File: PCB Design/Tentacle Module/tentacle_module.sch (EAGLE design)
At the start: 53 parts, among them IC1 5V, T1 NTD5867NL, T2 NTD5867NL, T3 NTD5867NL, T4 NTD5867NL, X3 RJ45-8X, X4 RJ45-8X

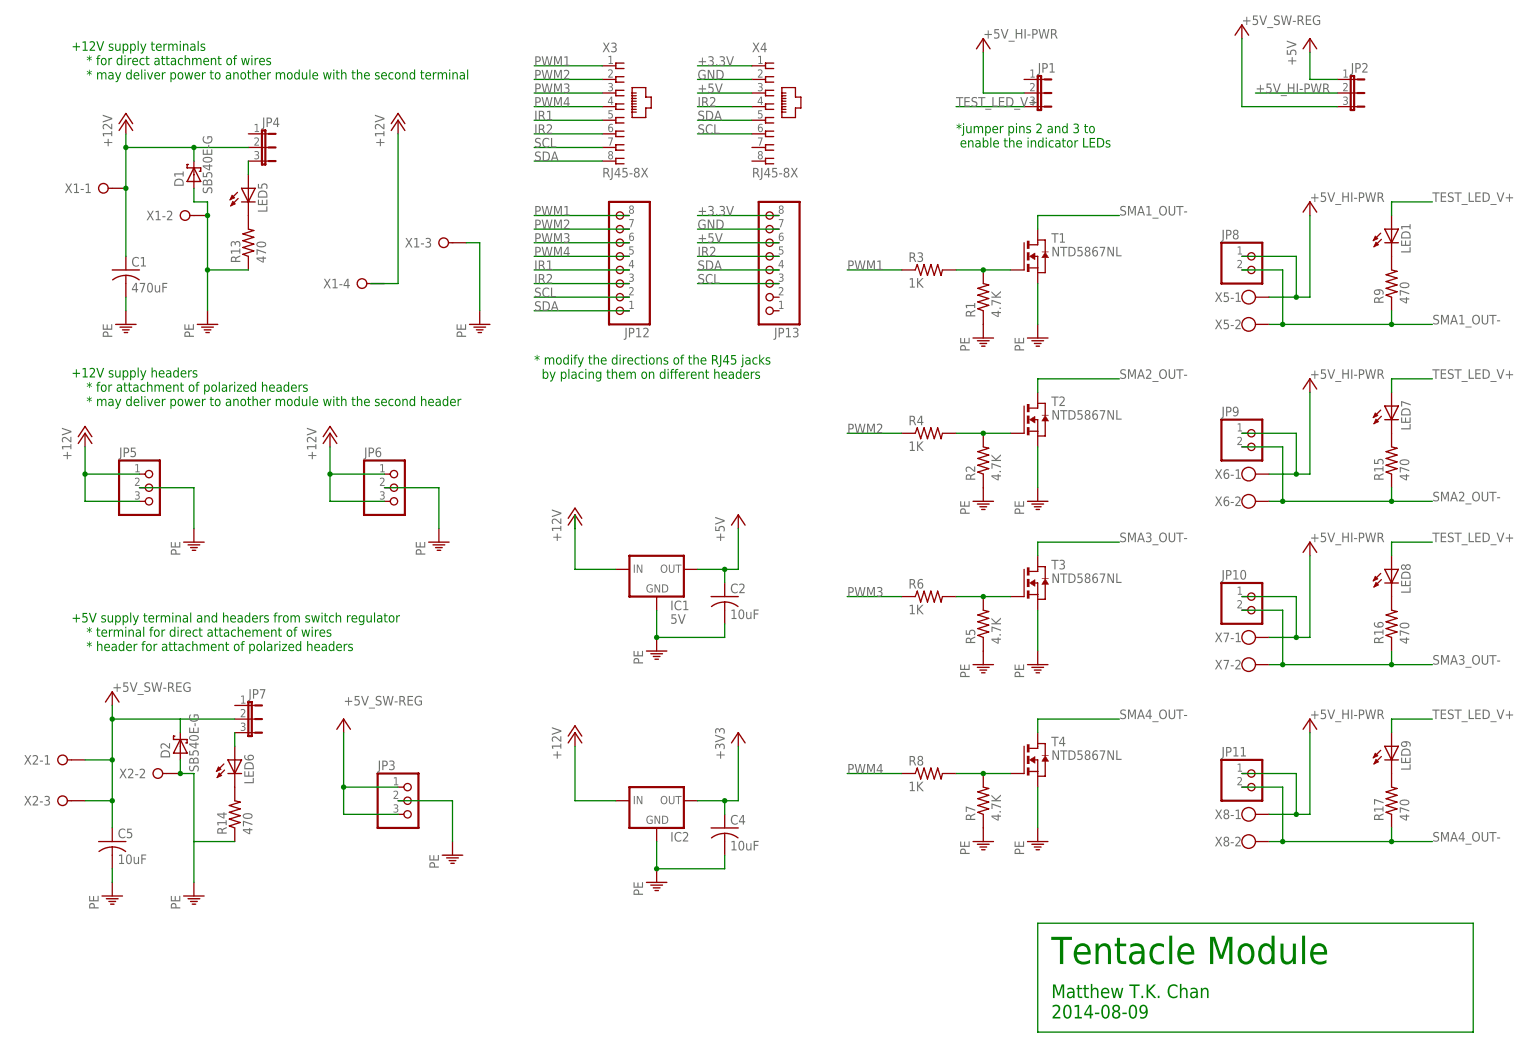
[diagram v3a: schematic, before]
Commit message: Updated the Tentacle module schematic
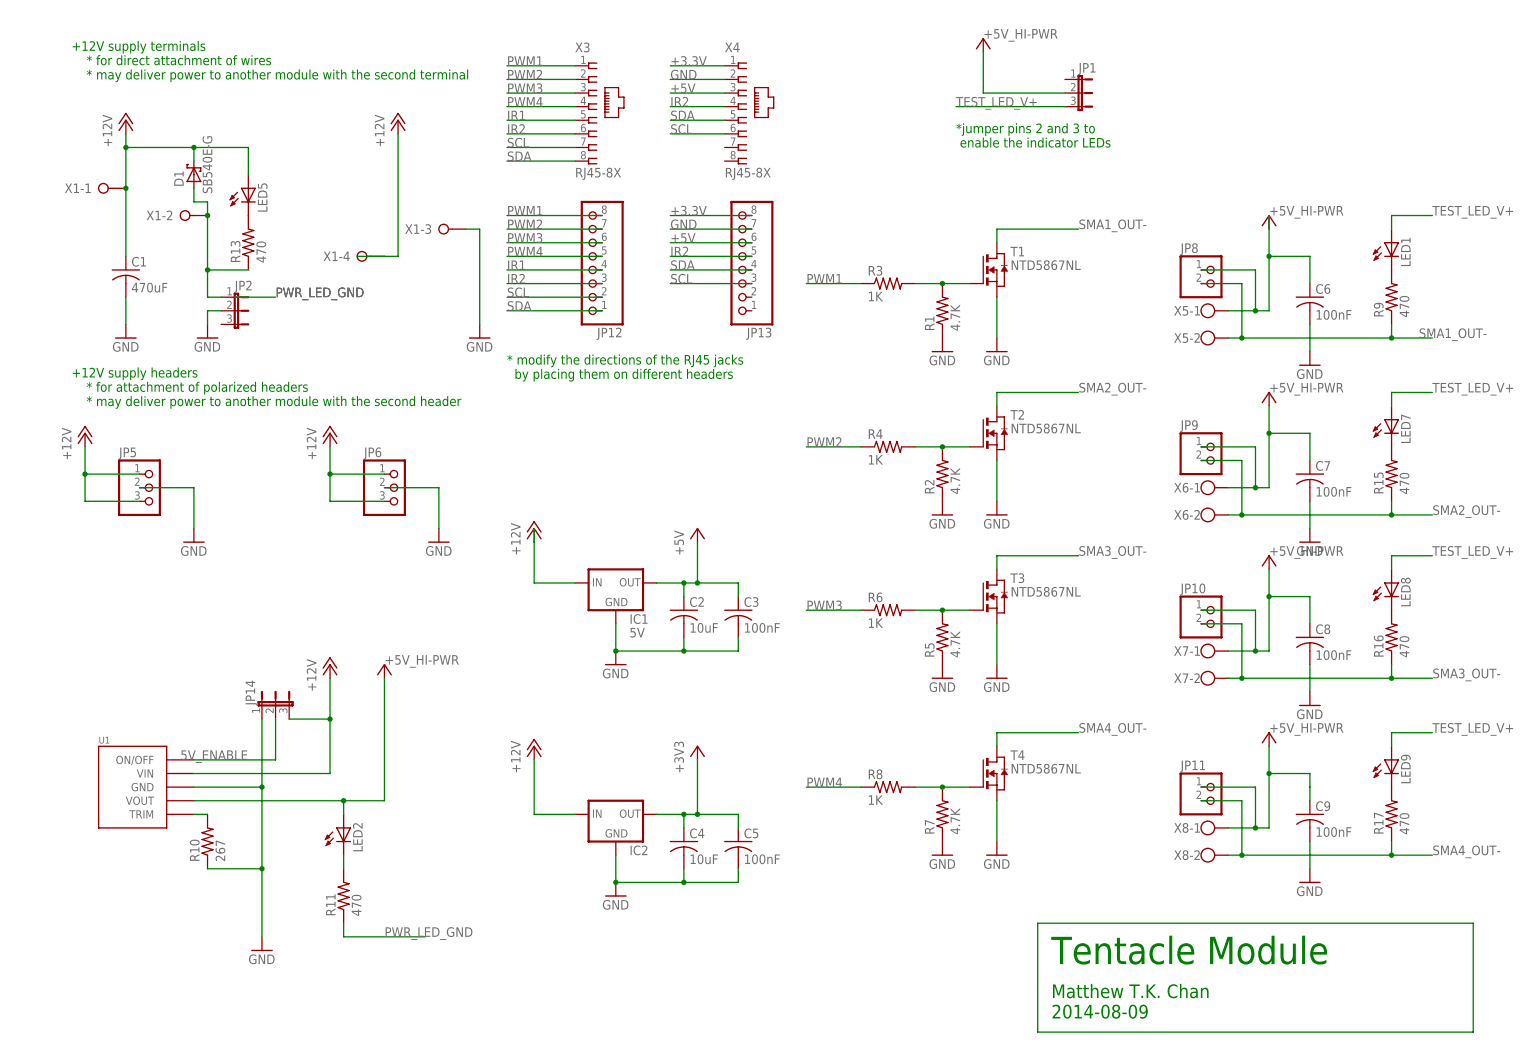
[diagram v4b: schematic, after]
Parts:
- removed D2: SB540E-G, CBLA_Test_bed_Library:SB540E-G
- removed JP3: (no value), CBLA_Test_bed_Library:PINHD-1X3/90
- removed JP4, JP7: (no value), jumper:JP2E
- removed LED6: (no value), led:LEDSML1206
- removed R14: 470, rcl:R-US_R1206
- removed X2: (no value), con-wago-508:W237-03P
- added C3, C6, C7, C8, C9: 100nF, rcl:C-USC0603
- added JP14: (no value), jumper:JP2E
- added LED2: (no value), led:LEDSML1206
- added R10: 267, CBLA_Test_bed_Library:R-US_R0603
- added R11: 470, CBLA_Test_bed_Library:R-US_R0603
- added U1: OKR-T/10-W12, CBLA_Test_bed_Library:OKR-T/10-W12
- C1, C2, C4: device rcl:C-USC1206 -> rcl:C-USC0603
- C5: value 10uF -> 100nF; device rcl:C-USC1206 -> rcl:C-USC0603
- R1, R13, R15, R16, R17, R2, R3, R4, R5, R6, R7, R8, R9: device rcl:R-US_R1206 -> CBLA_Test_bed_Library:R-US_R0603
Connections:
- removed net +12V1: JP7.2
- removed net +5V_SW-REG: C5.1, D2.C, JP3.1, JP3.3, X2-1.KL, X2-3.KL
- removed net GND1: R14.1
- removed net N$11: JP4.3, LED5.A
- removed net N$12: LED6.C, R14.2
- removed net N$13: JP7.3, LED6.A
- new net 5V_ENABLE: JP14.2, U1.ON/OFF
- new net N$6: R10.2, U1.TRIM
- new net N$7: LED2.C, R11.2
- new net PWR_LED_GND: D1.A, JP2.1, R11.1, R13.1, X1-2.KL
- net +12V: now also JP14.3, LED5.A, U1.VIN, X1-4.KL; no longer JP4.2
- net +3V3: now also C5.1
- net +5V: now also C3.1; no longer JP2.1, JP2.3
- net +5V_HI-PWR: now also C6.1, C7.1, C8.1, C9.1, LED2.A, U1.VOUT; no longer JP2.2
- net GND: now also C3.2, C6.2, C7.2, C8.2, C9.2, JP14.1, JP2.2, R10.1, U1.GND; no longer D1.A, D2.A, JP3.2, R13.1, X1-2.KL, X2-2.KL
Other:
- note removed: "+5V supply terminal and headers from switch regulator * terminal for direct attachement of wires * header for attachment of polarized headers"
- moved on the sheet: C2, C4, C5, IC1, IC2, JP1, JP10, JP11, JP12, JP13, JP2, JP8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

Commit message: Preliminary part placement for the tentacle board
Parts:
- removed IC2: (no value), CBLA_Test_bed_Library:78XXSHORIZONTAL
- added C10, C11: 10uF, rcl:C-USC0603
- added IC3: 3.3V, CBLA_Test_bed_Library:REG11173.3VDT
- IC1: value 5V -> 5.0V; device CBLA_Test_bed_Library:78XXSHORIZONTAL -> CBLA_Test_bed_Library:REG11175.0VDT
- JP12, JP13: device CBLA_Test_bed_Library:PINHD-1X8/90 -> CBLA_Test_bed_Library:PINHD-1X8
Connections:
- removed net N$15: LED8.C, R16.2
- removed net N$16: LED9.C, R17.2
- new net N$12: LED7.A, R15.1
- new net N$13: LED8.A, R16.1
- net +12V: now also C10.1, C11.1, IC1.VIN, IC3.VIN; no longer IC1.IN, IC2.IN
- net +3V3: now also IC3.VOUT; no longer IC2.OUT
- net +5V: now also IC1.VOUT; no longer IC1.OUT, JP1.2
- net +5V_HI-PWR: now also JP1.2
- net GND: now also C10.2, C11.2, IC3.GND; no longer IC2.GND
- net N$14: now also LED9.A, R17.1; no longer LED7.C, R15.2
- net N$5: now also LED1.A, R9.1; no longer LED1.C, R9.2
- net PWR_LED_GND: now also JP2.3; no longer JP2.1
- net SMA1_OUT-: now also LED1.C; no longer R9.1
- net SMA2_OUT-: now also LED7.C; no longer R15.1
- net SMA3_OUT-: now also LED8.C; no longer R16.1
- net SMA4_OUT-: now also LED9.C; no longer R17.1
- net TEST_LED_V+: now also R15.2, R16.2, R17.2, R9.2; no longer LED1.A, LED7.A, LED8.A, LED9.A
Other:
- moved on the sheet: JP2, JP6, LED1, LED7, LED8, LED9, R15, R16, R17, R9

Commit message: Finished routing the Tentacle module board
Not changing it!
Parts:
- added JP3: (no value), CBLA_Test_bed_Library:PINHD-1X3/90
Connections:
- removed net +3V3: C4.1, C5.1, IC3.VOUT
- net +3.3V: now also C4.1, C5.1, IC3.VOUT
- net +5V: now also JP3.2
- net GND: now also D1.A, JP3.3, X1-2.KL
- net IR1: now also JP3.1
- net PWR_LED_GND: no longer D1.A, X1-2.KL
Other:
- moved on the sheet: JP2, X1-2

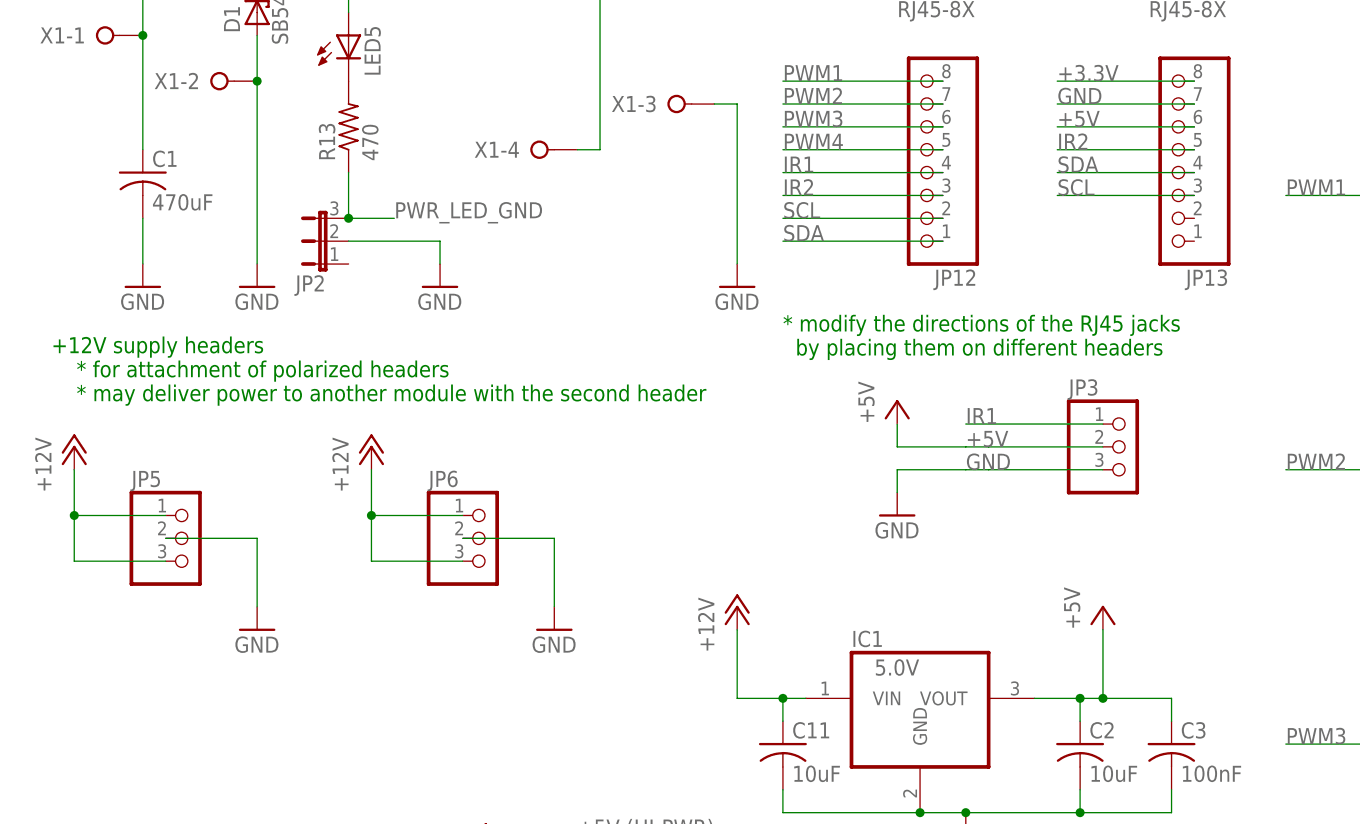
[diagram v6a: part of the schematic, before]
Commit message: made modifications to board design and correct errors
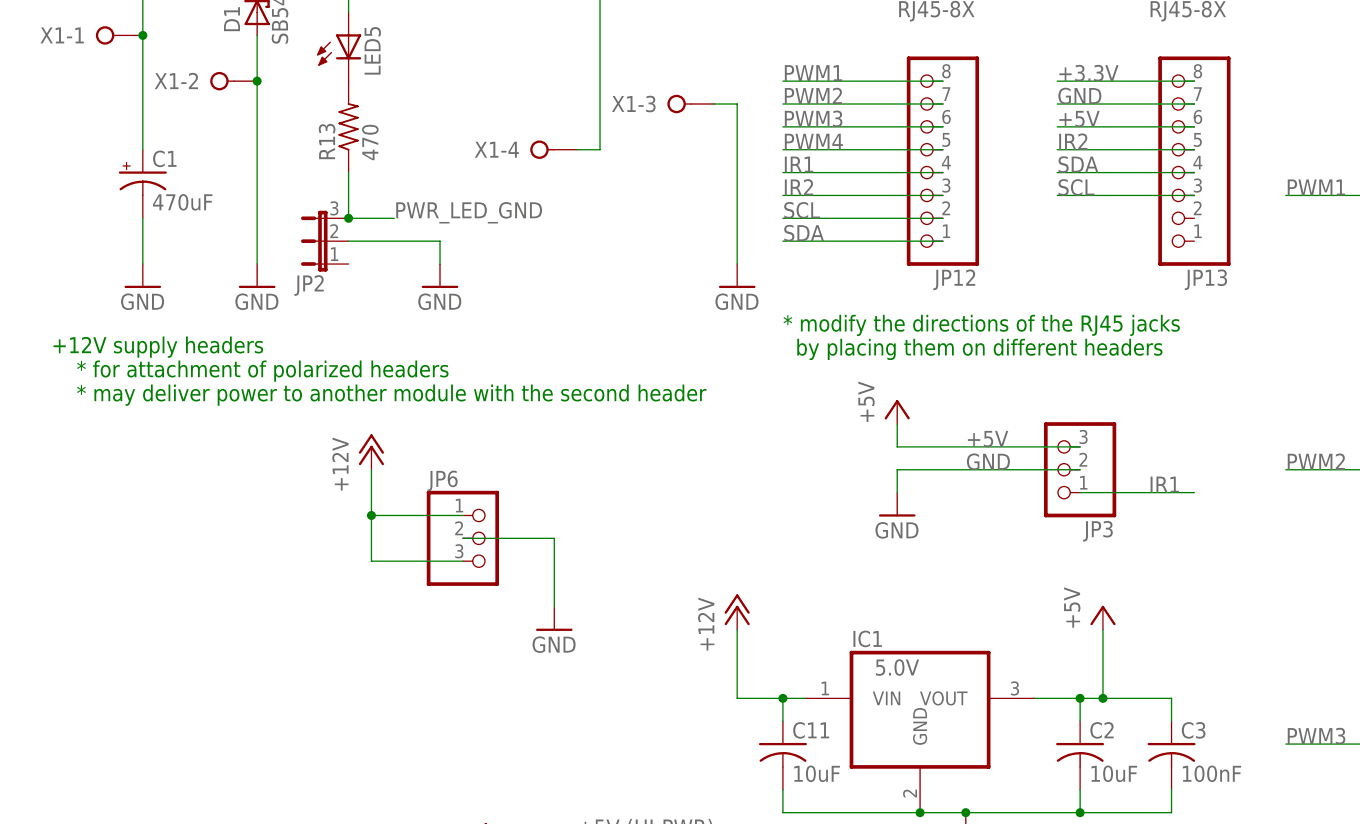
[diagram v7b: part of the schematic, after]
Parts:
- removed JP5: (no value), CBLA_Test_bed_Library:PINHD-1X3/90
- C1: device rcl:C-USC0603 -> rcl:CPOL-USE5-10.5
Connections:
- net +12V: now also C1.+; no longer C1.1, JP5.1, JP5.3
- net +5V: now also JP3.3; no longer JP3.2
- net GND: now also C1.-, JP3.2; no longer C1.2, JP3.3, JP5.2
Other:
- moved on the sheet: JP3
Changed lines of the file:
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@@
 <part name="JP1" library="jumper" deviceset="JP2E" device=""/>
 <part name="P+5" library="supply1" deviceset="+5V" device="" value="+5V (HI-PWR)"/>
-<part name="C1" library="rcl" deviceset="C-US" device="C0603" value="470uF"/>
+<part name="C1" library="rcl" deviceset="CPOL-US" device="E5-10.5" value="470uF"/>
 <part name="PE18" library="supply1" deviceset="GND" device=""/>
 <part name="PE19" library="supply1" deviceset="GND" device=""/>
-<part name="JP5" library="CBLA_Test_bed_Library" deviceset="PINHD-1X3" device="/90"/>
 <part name="PE20" library="supply1" deviceset="GND" device=""/>
-<part name="PE21" library="supply1" deviceset="GND" device=""/>
 <part name="JP6" library="CBLA_Test_bed_Library" deviceset="PINHD-1X3" device="/90"/>
 <part name="PE22" library="supply1" deviceset="GND" device=""/>
 <part name="P+14" library="supply1" deviceset="+12V" device=""/>
 <part name="P+15" library="supply1" deviceset="+12V" device=""/>
-<part name="P+16" library="supply1" deviceset="+12V" device=""/>
 <part name="P+11" library="supply1" deviceset="+5V" device="" value="+5V (HI-PWR)"/>
 <part name="D1" library="CBLA_Test_bed_Library" deviceset="SB540E-G" device=""/>
@@
 <instance part="PE18" gate="1" x="58.42" y="137.16"/>
 <instance part="PE19" gate="1" x="25.4" y="137.16"/>
-<instance part="JP5" gate="A" x="30.48" y="109.22"/>
 <instance part="PE20" gate="1" x="91.44" y="137.16"/>
-<instance part="PE21" gate="1" x="38.1" y="99.06"/>
 <instance part="JP6" gate="A" x="63.5" y="109.22"/>
 <instance part="PE22" gate="1" x="71.12" y="99.06"/>
 <instance part="P+14" gate="1" x="76.2" y="177.8"/>
 <instance part="P+15" gate="1" x="50.8" y="119.38"/>
-<instance part="P+16" gate="1" x="17.78" y="119.38"/>
 <instance part="P+11" gate="1" x="185.42" y="193.04" smashed="yes">
 <attribute name="VALUE" x="185.42" y="193.04" size="1.778" layer="96"/>
@@
 <instance part="C11" gate="G$1" x="96.52" y="86.36"/>
 <instance part="PE3" gate="1" x="38.1" y="137.16"/>
-<instance part="JP3" gate="A" x="134.62" y="119.38"/>
+<instance part="JP3" gate="A" x="127" y="116.84" rot="R180"/>
 <instance part="P+4" gate="VCC" x="109.22" y="124.46"/>
 <instance part="PE5" gate="1" x="109.22" y="111.76"/>
@@
 </segment>
 <segment>
-<pinref part="C1" gate="G$1" pin="1"/>
+<pinref part="C1" gate="G$1" pin="+"/>
 <pinref part="P+1" gate="1" pin="+12V"/>
 <wire x1="25.4" y1="175.26" x2="25.4" y2="172.72" width="0.1524" layer="91"/>
@@
 </segment>
 <segment>
-<pinref part="JP5" gate="A" pin="1"/>
-<wire x1="17.78" y1="116.84" x2="17.78" y2="111.76" width="0.1524" layer="91"/>
-<wire x1="17.78" y1="111.76" x2="27.94" y2="111.76" width="0.1524" layer="91"/>
-<pinref part="JP5" gate="A" pin="3"/>
-<wire x1="27.94" y1="106.68" x2="17.78" y2="106.68" width="0.1524" layer="91"/>
-<wire x1="17.78" y1="106.68" x2="17.78" y2="111.76" width="0.1524" layer="91"/>
-<junction x="17.78" y="111.76"/>
-<pinref part="P+16" gate="1" pin="+12V"/>
-</segment>
-<segment>
 <pinref part="U1" gate="G$1" pin="VIN"/>
 <pinref part="P+13" gate="1" pin="+12V"/>
@@
 <pinref part="P+4" gate="VCC" pin="VCC"/>
 <wire x1="109.22" y1="121.92" x2="109.22" y2="119.38" width="0.1524" layer="91"/>
-<pinref part="JP3" gate="A" pin="2"/>
-<wire x1="132.08" y1="119.38" x2="119.38" y2="119.38" width="0.1524" layer="91"/>
 <label x="116.84" y="119.38" size="1.778" layer="95"/>
-<wire x1="119.38" y1="119.38" x2="116.84" y2="119.38" width="0.1524" layer="91"/>
-<wire x1="109.22" y1="119.38" x2="116.84" y2="119.38" width="0.1524" layer="91"/>
+<pinref part="JP3" gate="A" pin="3"/>
+<wire x1="109.22" y1="119.38" x2="129.54" y2="119.38" width="0.1524" layer="91"/>
 </segment>
 </net>
@@
 <segment>
 <pinref part="JP3" gate="A" pin="1"/>
-<wire x1="132.08" y1="121.92" x2="116.84" y2="121.92" width="0.1524" layer="91"/>
-<label x="116.84" y="121.92" size="1.778" layer="95"/>
+<wire x1="129.54" y1="114.3" x2="142.24" y2="114.3" width="0.1524" layer="91"/>
+<label x="137.16" y="114.3" size="1.778" layer="95"/>
 </segment>
 </net>
@@
 </segment>
 <segment>
-<pinref part="C1" gate="G$1" pin="2"/>
+<pinref part="C1" gate="G$1" pin="-"/>
 <pinref part="PE19" gate="1" pin="GND"/>
 <wire x1="25.4" y1="144.78" x2="25.4" y2="139.7" width="0.1524" layer="91"/>
@@
 <wire x1="88.9" y1="157.48" x2="91.44" y2="157.48" width="0.1524" layer="91"/>
 <pinref part="X1" gate="-3" pin="KL"/>
-</segment>
-<segment>
-<pinref part="PE21" gate="1" pin="GND"/>
-<wire x1="38.1" y1="109.22" x2="38.1" y2="101.6" width="0.1524" layer="91"/>
-<pinref part="JP5" gate="A" pin="2"/>
-<wire x1="27.94" y1="109.22" x2="38.1" y2="109.22" width="0.1524" layer="91"/>
 </segment>
 <segment>
@@
 <pinref part="PE5" gate="1" pin="GND"/>
 <wire x1="109.22" y1="114.3" x2="109.22" y2="116.84" width="0.1524" layer="91"/>
-<pinref part="JP3" gate="A" pin="3"/>
-<wire x1="132.08" y1="116.84" x2="119.38" y2="116.84" width="0.1524" layer="91"/>
 <label x="116.84" y="116.84" size="1.778" layer="95"/>
-<wire x1="119.38" y1="116.84" x2="116.84" y2="116.84" width="0.1524" layer="91"/>
-<wire x1="109.22" y1="116.84" x2="116.84" y2="116.84" width="0.1524" layer="91"/>
-</segment>
-</net>
+<pinref part="JP3" gate="A" pin="2"/>
+<wire x1="109.22" y1="116.84" x2="129.54" y2="116.84" width="0.1524" layer="91"/>
+</segment>
+</net>
